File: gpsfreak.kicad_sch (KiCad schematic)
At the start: 1 part, among them J5 U.Fl

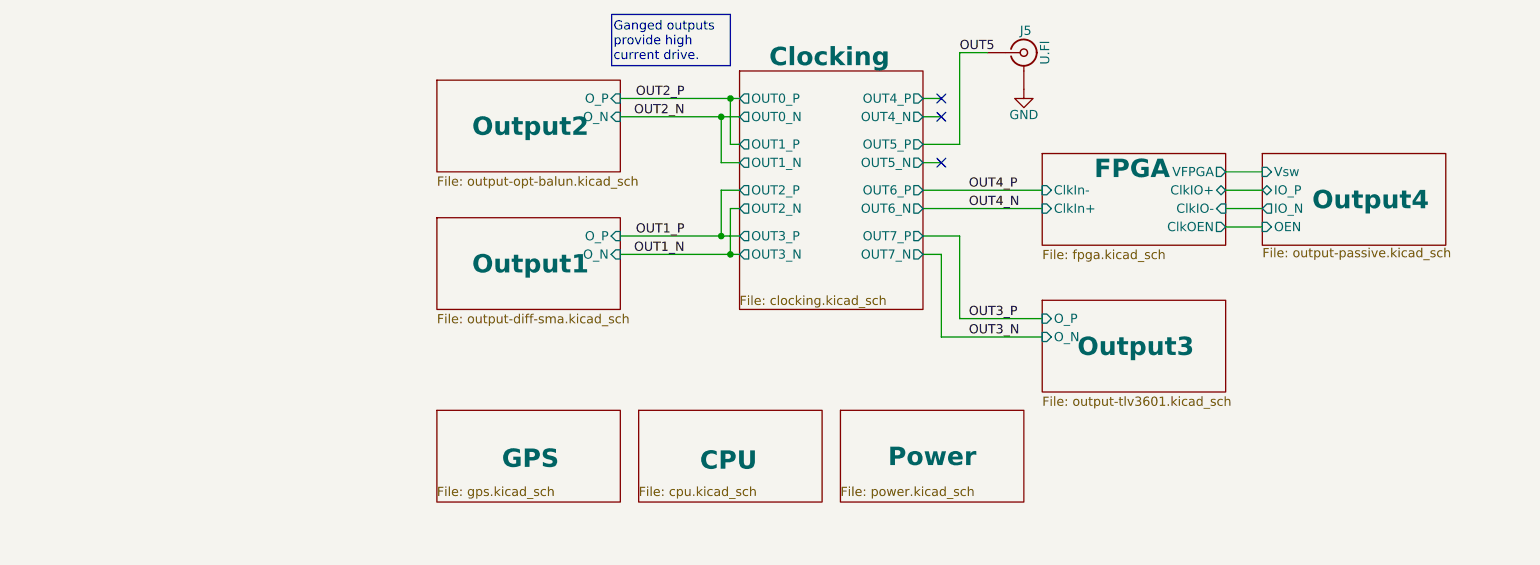
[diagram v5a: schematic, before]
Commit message: Adjustments.  Silk screen clearance.
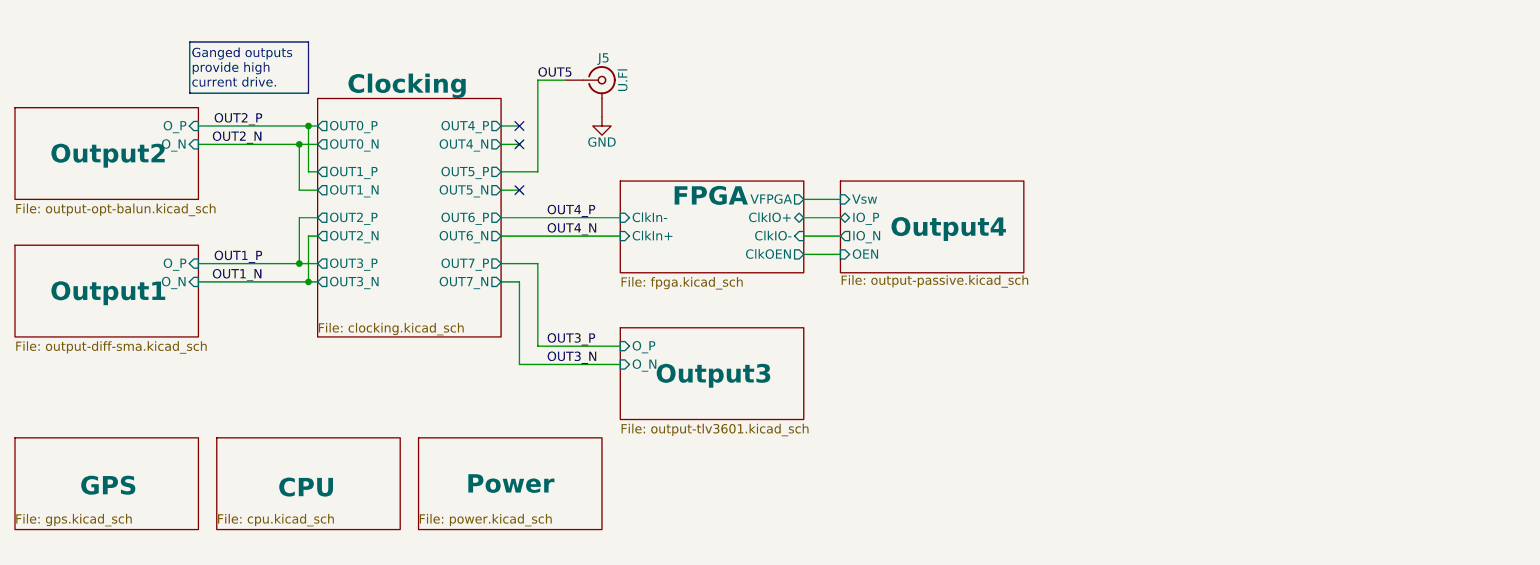
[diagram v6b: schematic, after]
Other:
- moved on the sheet: J5
